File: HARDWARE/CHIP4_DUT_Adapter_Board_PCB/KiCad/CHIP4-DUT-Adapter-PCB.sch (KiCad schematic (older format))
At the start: 13 parts, among them J5? CHIP4LH, J6? CHIP4RH

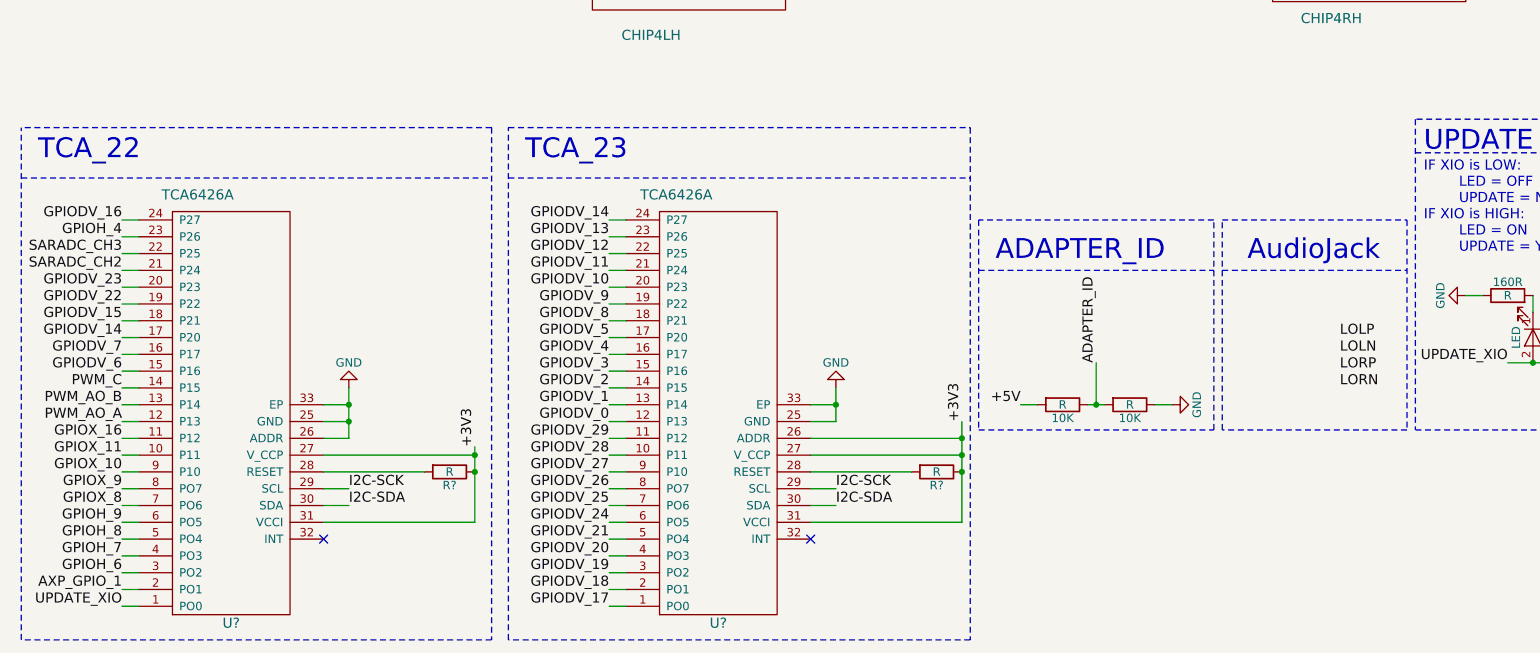
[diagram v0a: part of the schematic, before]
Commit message: updaing files, audio jack circuit
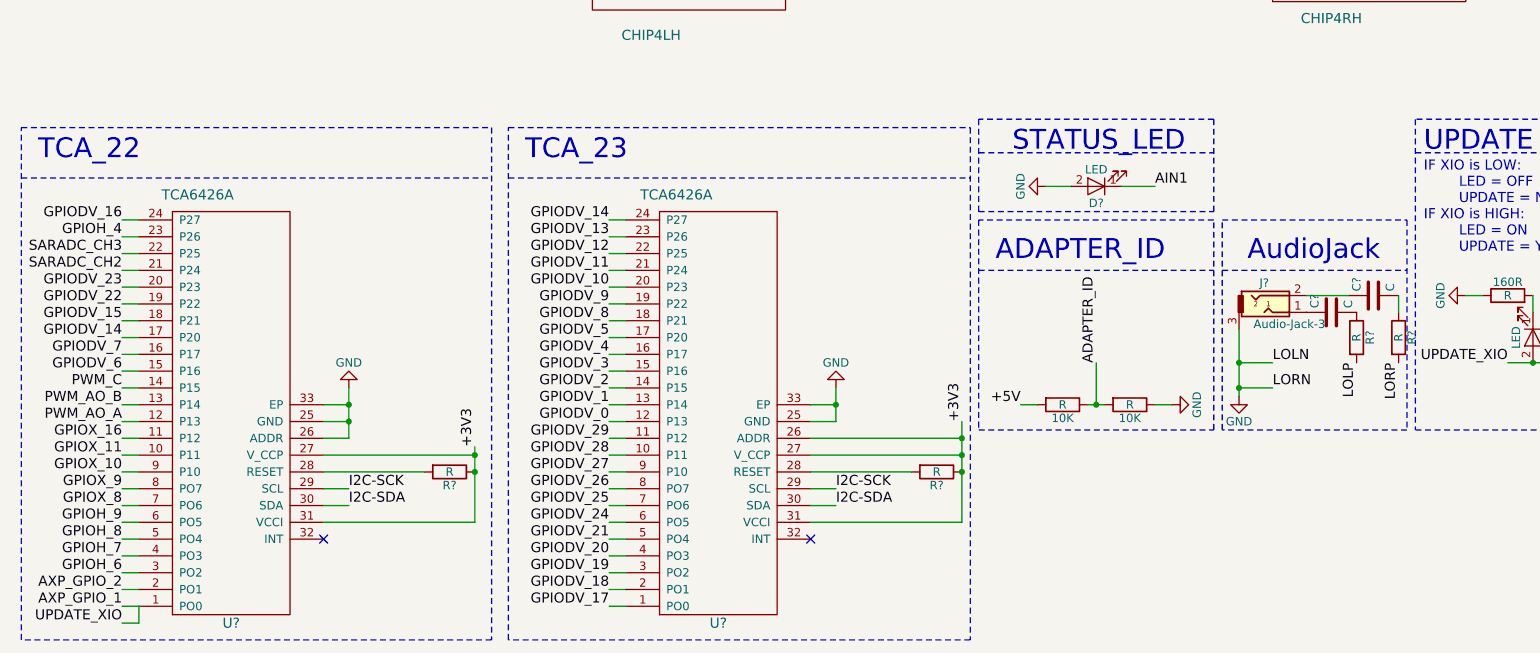
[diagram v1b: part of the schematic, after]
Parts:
- added C? (x2): C, symbol C
- added D?: LED, symbol LED
- added J?: Audio-Jack-3, symbol Audio-Jack-3
- added R? (x2): R, symbol R
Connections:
- net LOLN is gone; now on net GND: J6?.6 (LOLN)
- net LORN is gone; now on net GND: J6?.10 (LORN)
- net UPDATE_XIO is gone; now on net AXP_GPIO_1: D?.2 (A), Q?.1 (G), U?.1 (PO0)
- net AIN1: now also D?.1 (K)
- net AXP_GPIO_1: no longer U?.2 (PO1)
- net AXP_GPIO_2: now also U?.2 (PO1)
- net GND: now also D?.2 (A), J?.3
- net LOLP: now also R?.2
- net LORP: now also R?.2
- new net: C?.1, J?.1
- new net: C?.1, J?.2
- new net: C?.2, R?.1 (x2)
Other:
- note added: "STATUS_LED"

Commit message: updating to latest
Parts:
- gave numbers to parts that had none: 15
- renumbered 10K to 10K1, 10K to 10K2, 10K to 10K3, 160R to 160R1
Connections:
- net INA42_V-: no longer names the net of J1.11 (Pin_11)
- net INA43_V-: no longer names the net of J1.9 (Pin_9)
- no-connect marks 5 -> 7
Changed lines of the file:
@@
 $EndDescr
 $Comp
-L CHIP4LH J5?
+L CHIP4LH J51
 U 1 1 5A0612C4
 P 4500 4200
-F 0 "J5?" H 3950 6400 60  0000 C CNN
+F 0 "J51" H 3950 6400 60  0000 C CNN
 F 1 "CHIP4LH" H 4300 4050 60  0000 C CNN
 F 2 "" H 4600 4200 60  0001 C CNN
@@
 $EndComp
 $Comp
-L CHIP4RH J6?
+L CHIP4RH J61
 U 1 1 5A0613AD
 P 8600 4150
-F 0 "J6?" H 8100 6200 60  0000 C CNN
+F 0 "J61" H 8100 6200 60  0000 C CNN
 F 1 "CHIP4RH" H 8350 4050 60  0000 C CNN
 F 2 "" H 8650 4150 60  0001 C CNN
@@
 $EndComp
 $Comp
-L Conn_02x10_Counter_Clockwise J?
+L Conn_02x10_Counter_Clockwise J1
 U 1 1 5A0618EA
 P 1650 2950
-F 0 "J?" H 1700 3450 50  0000 C CNN
+F 0 "J1" H 1700 3450 50  0000 C CNN
 F 1 "CHIP4 DUT CONN" H 1700 2350 50  0000 C CNN
 F 2 "" H 1650 2950 50  0001 C CNN
@@
 AIN0
 $Comp
-L GND #PWR?
+L GND #PWR01
 U 1 1 5A0624D5
 P 900 2250
-F 0 "#PWR?" H 900 2000 50  0001 C CNN
+F 0 "#PWR01" H 900 2000 50  0001 C CNN
 F 1 "GND" H 900 2100 50  0000 C CNN
 F 2 "" H 900 2250 50  0001 C CNN
@@
 	-1   0    0    1
 $EndComp
-Text Label 1250 2600 1    60   ~ 0
-INA43_V-
-Text Label 1150 3400 3    60   ~ 0
-INA42_V-
 Text Label 1350 3400 3    60   ~ 0
 INA41_V-
@@
 I2C-SCK
 $Comp
-L GND #PWR?
+L GND #PWR02
 U 1 1 5A06285C
 P 3500 1850
-F 0 "#PWR?" H 3500 1600 50  0001 C CNN
+F 0 "#PWR02" H 3500 1600 50  0001 C CNN
 F 1 "GND" H 3500 1700 50  0000 C CNN
 F 2 "" H 3500 1850 50  0001 C CNN
@@
 $EndComp
 $Comp
-L GND #PWR?
+L GND #PWR03
 U 1 1 5A062877
 P 5550 1850
-F 0 "#PWR?" H 5550 1600 50  0001 C CNN
+F 0 "#PWR03" H 5550 1600 50  0001 C CNN
 F 1 "GND" H 5550 1700 50  0000 C CNN
 F 2 "" H 5550 1850 50  0001 C CNN
@@
 $EndComp
 $Comp
-L GND #PWR?
+L GND #PWR04
 U 1 1 5A06288B
 P 7550 1900
-F 0 "#PWR?" H 7550 1650 50  0001 C CNN
+F 0 "#PWR04" H 7550 1650 50  0001 C CNN
 F 1 "GND" H 7550 1750 50  0000 C CNN
 F 2 "" H 7550 1900 50  0001 C CNN
@@
 $EndComp
 $Comp
-L GND #PWR?
+L GND #PWR05
 U 1 1 5A06289F
 P 9600 1900
-F 0 "#PWR?" H 9600 1650 50  0001 C CNN
+F 0 "#PWR05" H 9600 1650 50  0001 C CNN
 F 1 "GND" H 9600 1750 50  0000 C CNN
 F 2 "" H 9600 1900 50  0001 C CNN
@@
 AIN3
 $Comp
-L TCA6426A U?
+L TCA6426A U1
 U 1 1 5A063163
 P 1700 7000
-F 0 "U?" H 1600 7850 60  0000 C CNN
+F 0 "U1" H 1600 7850 60  0000 C CNN
 F 1 "TCA6426A" H 1800 5300 60  0000 C CNN
 F 2 "" H 1700 7000 60  0001 C CNN
@@
 SARADC_CH3
 $Comp
-L TCA6426A U?
+L TCA6426A U2
 U 1 1 5A065B58
 P 4600 7000
-F 0 "U?" H 4500 7850 60  0000 C CNN
+F 0 "U2" H 4500 7850 60  0000 C CNN
 F 1 "TCA6426A" H 4750 5300 60  0000 C CNN
 F 2 "" H 4600 7000 60  0001 C CNN
@@
 I2C-SDA
 $Comp
-L GND #PWR?
+L GND #PWR06
 U 1 1 5A0674FC
 P 2500 6450
-F 0 "#PWR?" H 2500 6200 50  0001 C CNN
+F 0 "#PWR06" H 2500 6200 50  0001 C CNN
 F 1 "GND" H 2500 6300 50  0000 C CNN
 F 2 "" H 2500 6450 50  0001 C CNN
@@
 +3V3
 $Comp
-L R R?
+L R R3
 U 1 1 5A0679EC
 P 3100 6950
-F 0 "R?" V 3180 6950 50  0000 C CNN
+F 0 "R3" V 3180 6950 50  0000 C CNN
 F 1 "R" V 3100 6950 50  0000 C CNN
 F 2 "" V 3030 6950 50  0001 C CNN
@@
 I2C-SDA
 $Comp
-L GND #PWR?
+L GND #PWR07
 U 1 1 5A068567
 P 5400 6450
-F 0 "#PWR?" H 5400 6200 50  0001 C CNN
+F 0 "#PWR07" H 5400 6200 50  0001 C CNN
 F 1 "GND" H 5400 6300 50  0000 C CNN
 F 2 "" H 5400 6450 50  0001 C CNN
@@
 +3V3
 $Comp
-L R R?
+L R R4
 U 1 1 5A068572
 P 6000 6950
-F 0 "R?" V 6080 6950 50  0000 C CNN
+F 0 "R4" V 6080 6950 50  0000 C CNN
 F 1 "R" V 6000 6950 50  0000 C CNN
 F 2 "" V 5930 6950 50  0001 C CNN
@@
 NoConn ~ 5250 7350
 $Comp
-L R 10K
+L R 10K1
 U 1 1 5A069970
 P 5850 2250
-F 0 "10K" V 5930 2250 50  0000 C CNN
+F 0 "10K1" V 5930 2250 50  0000 C CNN
 F 1 "R" V 5850 2250 50  0000 C CNN
 F 2 "" V 5780 2250 50  0001 C CNN
@@
 ADAPTER_ID
 $Comp
-L R 10K
+L R 10K2
 U 1 1 5A069CCA
 P 6750 6550
-F 0 "10K" V 6830 6550 50  0000 C CNN
+F 0 "10K2" V 6830 6550 50  0000 C CNN
 F 1 "R" V 6750 6550 50  0000 C CNN
 F 2 "" V 6680 6550 50  0001 C CNN
@@
 $EndComp
 $Comp
-L R 10K
+L R 10K3
 U 1 1 5A069DDE
 P 7150 6550
-F 0 "10K" V 7230 6550 50  0000 C CNN
+F 0 "10K3" V 7230 6550 50  0000 C CNN
 F 1 "R" V 7150 6550 50  0000 C CNN
 F 2 "" V 7080 6550 50  0001 C CNN
@@
 $EndComp
 $Comp
-L GND #PWR?
+L GND #PWR08
 U 1 1 5A069E20
 P 7400 6550
-F 0 "#PWR?" H 7400 6300 50  0001 C CNN
+F 0 "#PWR08" H 7400 6300 50  0001 C CNN
 F 1 "GND" H 7400 6400 50  0000 C CNN
 F 2 "" H 7400 6550 50  0001 C CNN
@@
 UPDATE
 $Comp
-L LED D?
+L LED D2
 U 1 1 5A06BCE2
 P 9550 6150
-F 0 "D?" H 9550 6250 50  0000 C CNN
+F 0 "D2" H 9550 6250 50  0000 C CNN
 F 1 "LED" H 9550 6050 50  0000 C CNN
 F 2 "" H 9550 6150 50  0001 C CNN
@@
 $EndComp
 $Comp
-L Q_NMOS_GDSD Q?
+L Q_NMOS_GDSD Q1
 U 1 1 5A06BDA9
 P 9850 6300
-F 0 "Q?" H 10050 6350 50  0000 L CNN
+F 0 "Q1" H 10050 6350 50  0000 L CNN
 F 1 "ZXMN4A06GT" H 10050 6250 50  0000 L CNN
 F 2 "" H 10050 6400 50  0001 C CNN
@@
 $EndComp
 $Comp
-L GND #PWR?
+L GND #PWR09
 U 1 1 5A06BF66
 P 9950 6600
-F 0 "#PWR?" H 9950 6350 50  0001 C CNN
+F 0 "#PWR09" H 9950 6350 50  0001 C CNN
 F 1 "GND" H 9950 6450 50  0000 C CNN
 F 2 "" H 9950 6600 50  0001 C CNN
@@
 UPDATE_XIO
 $Comp
-L R 160R
+L R 160R1
 U 1 1 5A06C5DC
 P 9400 5900
-F 0 "160R" V 9480 5900 50  0000 C CNN
+F 0 "160R1" V 9480 5900 50  0000 C CNN
 F 1 "R" V 9400 5900 50  0000 C CNN
 F 2 "" V 9330 5900 50  0001 C CNN
@@
 $EndComp
 $Comp
-L GND #PWR?
+L GND #PWR010
 U 1 1 5A06C90B
 P 9150 5900
-F 0 "#PWR?" H 9150 5650 50  0001 C CNN
+F 0 "#PWR010" H 9150 5650 50  0001 C CNN
 F 1 "GND" H 9150 5750 50  0000 C CNN
 F 2 "" H 9150 5900 50  0001 C CNN
@@
 Connection ~ 1250 3300
 Wire Wire Line
-	1250 2750 1250 2600
-Wire Wire Line
 	2050 3400 2050 3250
 Wire Wire Line
@@
 Wire Wire Line
 	1350 3400 1350 3250
-Wire Wire Line
-	1150 3400 1150 3250
 Wire Wire Line
 	9600 1900 9600 4100
@@
 	1250 7850 1250 7750
 $Comp
-L LED D?
+L LED D1
 U 1 1 5A062FFF
 P 6950 5250
-F 0 "D?" H 6950 5350 50  0000 C CNN
+F 0 "D1" H 6950 5350 50  0000 C CNN
 F 1 "LED" H 6950 5150 50  0000 C CNN
 F 2 "" H 6950 5250 50  0001 C CNN
@@
 $EndComp
 $Comp
-L GND #PWR?
+L GND #PWR011
 U 1 1 5A063080
 P 6650 5250
-F 0 "#PWR?" H 6650 5000 50  0001 C CNN
+F 0 "#PWR011" H 6650 5000 50  0001 C CNN
 F 1 "GND" H 6650 5100 50  0000 C CNN
 F 2 "" H 6650 5250 50  0001 C CNN
@@
 	6250 5050 7650 5050
 $Comp
-L Audio-Jack-3 J?
+L Audio-Jack-3 J2
 U 1 1 5A063866
 P 8000 6000
-F 0 "J?" H 7950 6175 50  0000 C CNN
+F 0 "J2" H 7950 6175 50  0000 C CNN
 F 1 "Audio-Jack-3" H 8100 5930 50  0000 C CNN
 F 2 "" H 8250 6100 50  0001 C CNN
@@
 $EndComp
 $Comp
-L R R?
+L R R2
 U 1 1 5A063B8F
 P 8750 6150
-F 0 "R?" V 8830 6150 50  0000 C CNN
+F 0 "R2" V 8830 6150 50  0000 C CNN
 F 1 "R" V 8750 6150 50  0000 C CNN
 F 2 "" V 8680 6150 50  0001 C CNN
@@
 $EndComp
 $Comp
-L C C?
+L C C1
 U 1 1 5A063C00
 P 8600 5900
-F 0 "C?" H 8625 6000 50  0000 L CNN
+F 0 "C1" H 8625 6000 50  0000 L CNN
 F 1 "C" H 8625 5800 50  0000 L CNN
 F 2 "" H 8638 5750 50  0001 C CNN
@@
 	8450 5900 8200 5900
 $Comp
-L R R?
+L R R1
 U 1 1 5A063E13
 P 8500 6150
-F 0 "R?" V 8580 6150 50  0000 C CNN
+F 0 "R1" V 8580 6150 50  0000 C CNN
 F 1 "R" V 8500 6150 50  0000 C CNN
 F 2 "" V 8430 6150 50  0001 C CNN
@@
 $EndComp
 $Comp
-L C C?
+L C C2
 U 1 1 5A063E67
 P 8350 6000
-F 0 "C?" H 8375 6100 50  0000 L CNN
+F 0 "C2" H 8375 6100 50  0000 L CNN
 F 1 "C" H 8375 5900 50  0000 L CNN
 F 2 "" H 8388 5850 50  0001 C CNN
@@
 $EndComp
 $Comp
-L GND #PWR?
+L GND #PWR012
 U 1 1 5A063F2F
 P 7800 6500
-F 0 "#PWR?" H 7800 6250 50  0001 C CNN
+F 0 "#PWR012" H 7800 6250 50  0001 C CNN
 F 1 "GND" H 7800 6350 50  0000 C CNN
 F 2 "" H 7800 6500 50  0001 C CNN
@@
 Wire Wire Line
 	8750 6000 8750 5900
+NoConn ~ 1150 3250
+NoConn ~ 1250 2750
 $EndSCHEMATC
